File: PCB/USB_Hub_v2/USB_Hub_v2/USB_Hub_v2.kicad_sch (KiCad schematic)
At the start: 45 parts, among them J1 USB_A, J2 USB_A, J3 USB_A, J4 USB_A, J5 USB_A, J6 USB_A, SW1 SW_Push_DPDT, U1 FE1.1s, U2 TS3USB30EDGSR, U3 TPS2116DRL, U4 USBLC6-2SC6, U5 USBLC6-2SC6, U6 USBLC6-2SC6, U7 USBLC6-2SC6, U8 USBLC6-2SC6, U9 USBLC6-2SC6, Y1 Crystal

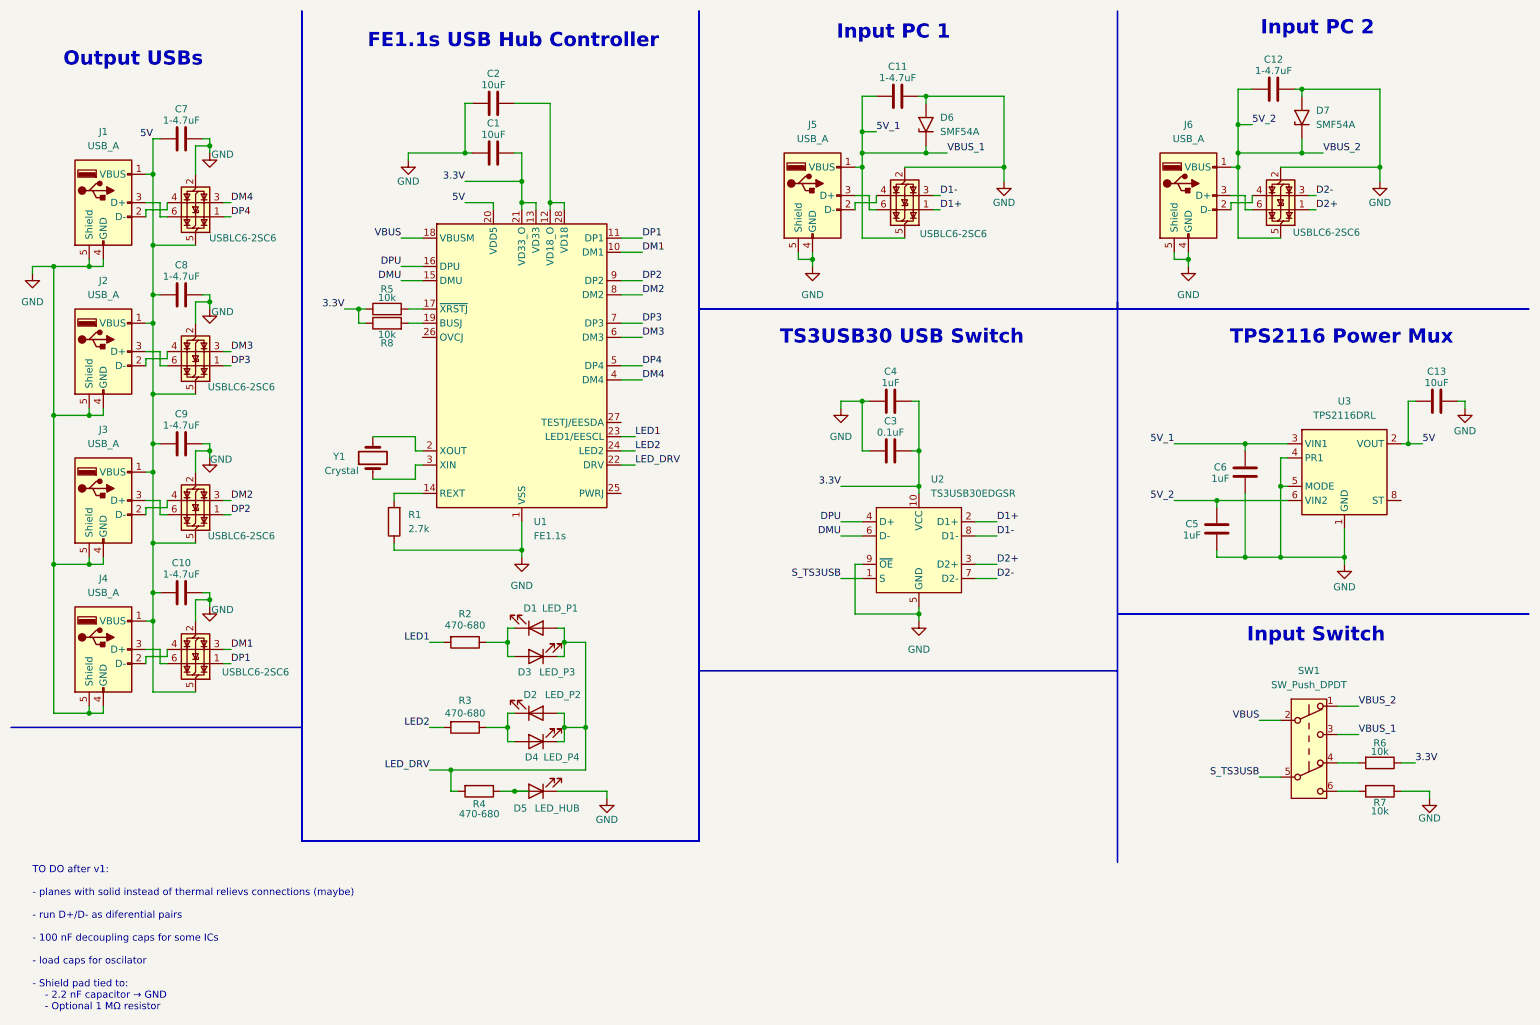
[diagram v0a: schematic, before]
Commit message: Update PCB layout: stackup, nets and footprints
Add recent PCB backup archives and apply extensive KiCad PCB updates: define board stackup and layer types (B.Cu -> power), rename/reorder nets, and replace/update multiple footprints and component properties (resistors, capacitors, pads, models, references and values). Adjust pad positions, sizes and net assignments, update 3D model links and footprint metadata to match revised layout. These changes appear to be automated footprint/housekeeping edits and netlist/stack adjustments to prepare the board for updated fabrication/assembly.
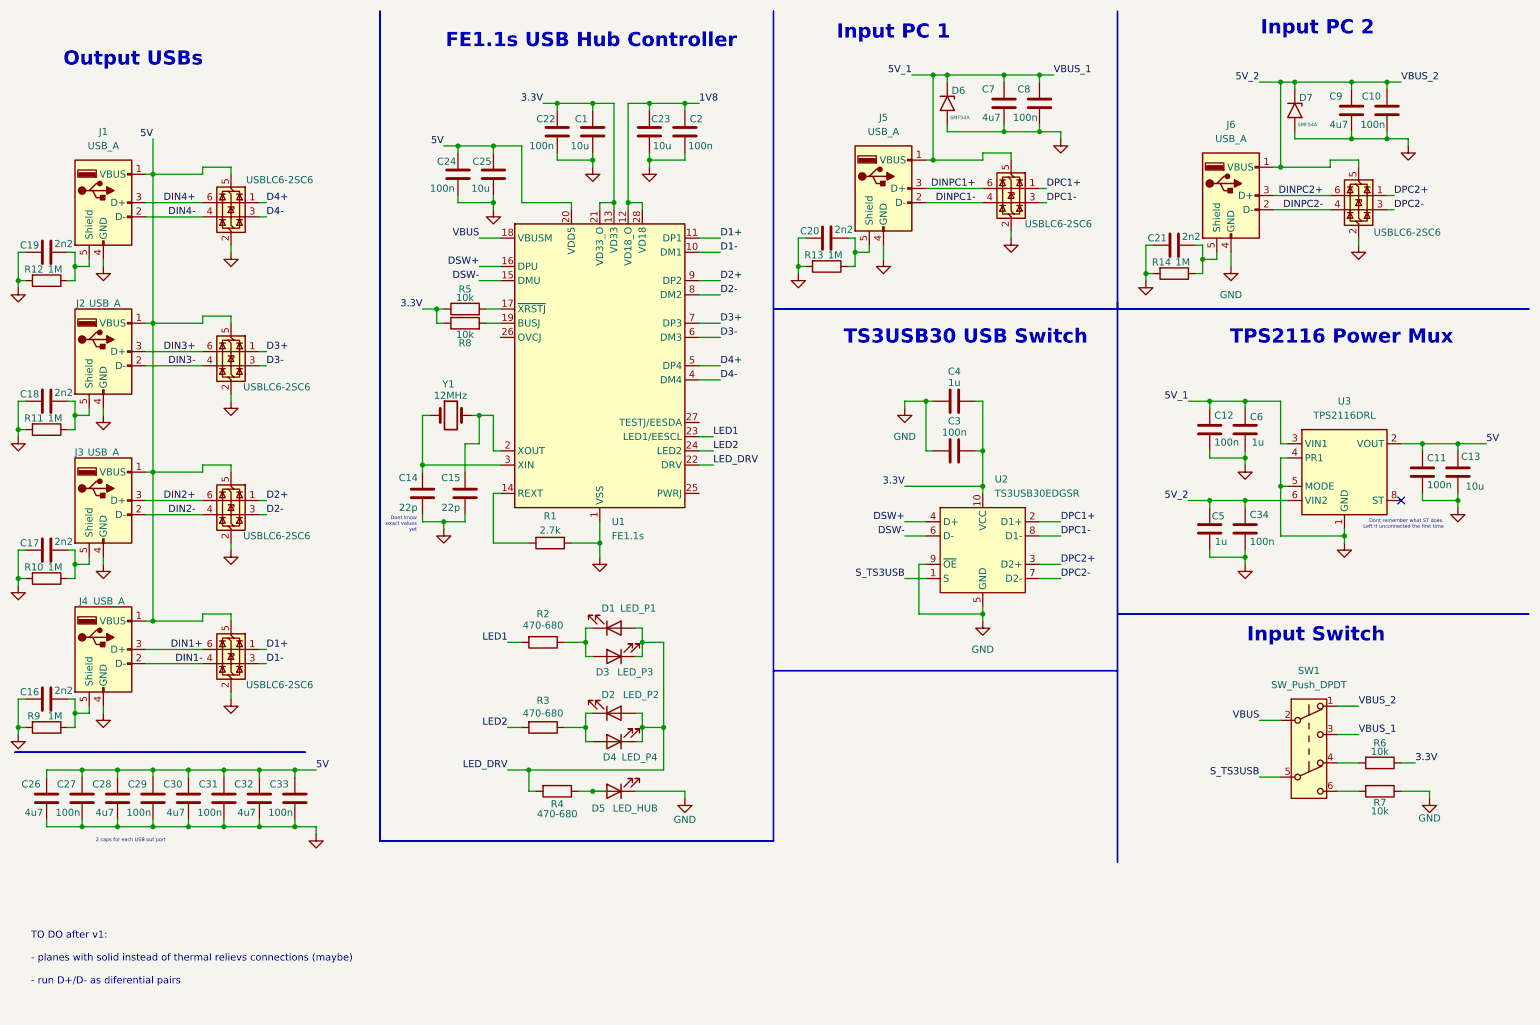
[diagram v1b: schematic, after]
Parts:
- added C14, C15: 22p, Capacitor_SMD:C_0805_2012Metric_Pad1.18x1.45mm_HandSolder, symbol Device:C
- added C16, C17, C18, C19, C20, C21: 2n2, Capacitor_SMD:C_0805_2012Metric_Pad1.18x1.45mm_HandSolder, symbol Device:C
- added C22, C24, C27, C29, C31, C33, C34: 100n, Capacitor_SMD:C_0805_2012Metric_Pad1.18x1.45mm_HandSolder, symbol Device:C
- added C23, C25: 10u, Capacitor_SMD:C_0805_2012Metric_Pad1.18x1.45mm_HandSolder, symbol Device:C
- added C26, C28, C30, C32: 4u7, Capacitor_SMD:C_0805_2012Metric_Pad1.18x1.45mm_HandSolder, symbol Device:C
- added R10, R11, R12, R13, R14, R9: 1M, Resistor_SMD:R_0603_1608Metric_Pad0.98x0.95mm_HandSolder, symbol Device:R
- C1, C13: value 10uF -> 10u
- C10, C11, C12, C8: value 1-4.7uF -> 100n
- C2: value 10uF -> 100n
- C3: value 0.1uF -> 100n
- C4, C5, C6: value 1uF -> 1u
- C7, C9: value 1-4.7uF -> 4u7
- Y1: value Crystal -> 12MHz
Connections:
- net DM1 is gone; now on net D1-: U1.10 (DM1), U7.3 (I/O2)
- net DM2 is gone; now on net D2-: U1.8 (DM2), U6.3 (I/O2)
- net DP1 is gone; now on net D1+: U1.11 (DP1), U7.1 (I/O1)
- net DP2 is gone; now on net D2+: U1.9 (DP2), U6.1 (I/O1)
- net 3.3V: now also C22.2
- net 5V: now also C11.1, C13.2, C24.2, C25.2, C26.2, C27.2, C28.2, C29.2, C30.2, C31.2, C32.2, C33.2; no longer C10.1, C13.1, C7.1, C8.1, C9.1
- net 5V_1: now also C12.1, C7.2, C8.2; no longer C11.1
- net 5V_2: now also C10.2, C9.2, C34.1; no longer C12.1
- net D1+: no longer U2.2 (D1+), U8.1 (I/O1)
- net D1-: no longer U2.8 (D1-), U8.3 (I/O2)
- net D2+: no longer U2.3 (D2+), U9.1 (I/O1)
- net D2-: no longer U2.7 (D2-), U9.3 (I/O2)
- net GND: now also C10.1, C13.1, C7.1, C8.1, C9.1, C14.1, C15.1, C16.1, C17.1, C18.1, C19.1, C20.1, C21.1, C22.1, C23.1, C24.1, C25.1, C26.1, C27.1, C28.1, C29.1, C30.1, C31.1, C32.1, C33.1, C34.2, R10.2, R11.2, R12.2, R13.2, R14.2, R9.2; no longer C10.2, C13.2, C7.2, C8.2, C9.2, J1.5 (Shield), J2.5 (Shield), J3.5 (Shield), J4.5 (Shield), J5.5 (Shield), J6.5 (Shield)
- net DINPC2-: now reaches J6.2 (D-), U9.4 (I/O2)
- net DINPC2+: now reaches J6.3 (D+), U9.6 (I/O1)
- net 1V8: now reaches C2.2, U1.12 (VD18_O), U1.28 (VD18)
- net 1V8: now also C23.2
- net DIN2-: now reaches J3.2 (D-), U6.4 (I/O2)
- net DIN2+: now reaches J3.3 (D+), U6.6 (I/O1)
- net DIN3-: now reaches J2.2 (D-), U5.4 (I/O2)
- net DIN3+: now reaches J2.3 (D+), U5.6 (I/O1)
- net DINPC1-: now reaches J5.2 (D-), U8.4 (I/O2)
- net DINPC1+: now reaches J5.3 (D+), U8.6 (I/O1)
- net at U1.2 (XOUT), Y1.2: now also C15.2
- net at U1.3 (XIN), Y1.1: now also C14.2
- net DIN1-: now reaches J4.2 (D-), U7.4 (I/O2)
- net DIN1+: now reaches J4.3 (D+), U7.6 (I/O1)
- net DIN4-: now reaches J1.2 (D-), U4.4 (I/O2)
- net DIN4+: now reaches J1.3 (D+), U4.6 (I/O1)
- net DM3 renamed D3-
- net DM4 renamed D4-
- net DMU renamed DSW-
- net DP3 renamed D3+
- net DP4 renamed D4+
- net DPU renamed DSW+
- new net: C17.2, J3.5 (Shield), R10.1
- new net: C21.2, J6.5 (Shield), R14.1
- new net: C20.2, J5.5 (Shield), R13.1
- new net: C16.2, J4.5 (Shield), R9.1
- new net: C18.2, J2.5 (Shield), R11.1
- new net: C19.2, J1.5 (Shield), R12.1
- new net DPC1+: U2.2 (D1+), U8.1 (I/O1)
- new net DPC1-: U2.8 (D1-), U8.3 (I/O2)
- new net DPC2+: U2.3 (D2+), U9.1 (I/O1)
- new net DPC2-: U2.7 (D2-), U9.3 (I/O2)
- no-connect marks 0 -> 1
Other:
- note added: "2 caps for each USB out port"
- note added: "Dont know exact values yet"
- note added: "Dont remember what ST does. Left it unconnected the first time"
- note added: "TO DO after v1: - planes with solid instead of thermal relievs connections (maybe) - run D+/D- as diferential pairs"
- note removed: "TO DO after v1: - planes with solid instead of thermal relievs connections (maybe) - run D+/D- as diferential pairs - 100 nF decoupling caps for some ICs - load caps for oscilator - Shield pad tied to: - 2.2 nF capacitor → GND - Optional 1 MΩ resistor"
- moved on the sheet: C1, C13, C3, C4, C5, C6, D1, D2, D3, D4, D5, D6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

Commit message: Adjust KiCad footprints and add backups
Rotate/reposition multiple SMD footprints, update pad rotations, fp_line/fp_text orientations and UUIDs in USB_Hub_v2.kicad_pcb (and related project files). Also update USB_Hub_v2.kicad_pro/.kicad_sch metadata to match footprint changes. Add five timestamped backup ZIPs under USB_Hub_v2-backups. These edits correct component orientations/placements and record backups.
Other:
- moved on the sheet: C2, C23
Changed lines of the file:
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@@
 	(symbol
 		(lib_id "Device:C")
-		(at 127 34.29 0)
+		(at 133.35 34.29 0)
 		(mirror x)
 		(unit 1)
@@
 		(dnp no)
 		(property "Reference" "C23"
-			(at 129.032 32.004 0)
+			(at 135.382 32.004 0)
 			(effects
 				(font
@@
 		)
 		(property "Value" "10u"
-			(at 129.286 36.83 0)
+			(at 135.636 36.83 0)
 			(effects
 				(font
@@
 		)
 		(property "Footprint" "Capacitor_SMD:C_0805_2012Metric_Pad1.18x1.45mm_HandSolder"
-			(at 127.9652 30.48 0)
+			(at 134.3152 30.48 0)
 			(effects
 				(font
@@
 		)
 		(property "Datasheet" "~"
-			(at 127 34.29 0)
+			(at 133.35 34.29 0)
 			(effects
 				(font
@@
 		)
 		(property "Description" "Unpolarized capacitor"
-			(at 127 34.29 0)
+			(at 133.35 34.29 0)
 			(effects
 				(font
@@
 	(symbol
 		(lib_id "Device:C")
-		(at 133.35 34.29 0)
+		(at 127 34.29 0)
 		(mirror x)
 		(unit 1)
@@
 		(dnp no)
 		(property "Reference" "C2"
-			(at 135.382 32.004 0)
+			(at 129.032 32.004 0)
 			(effects
 				(font
@@
 		)
 		(property "Value" "100n"
-			(at 136.144 36.83 0)
+			(at 129.794 36.83 0)
 			(effects
 				(font
@@
 		)
 		(property "Footprint" "Capacitor_SMD:C_0805_2012Metric_Pad1.18x1.45mm_HandSolder"
-			(at 134.3152 30.48 0)
+			(at 127.9652 30.48 0)
 			(effects
 				(font
@@
 		)
 		(property "Datasheet" "~"
-			(at 133.35 34.29 0)
+			(at 127 34.29 0)
 			(effects
 				(font
@@
 		)
 		(property "Description" "Unpolarized capacitor"
-			(at 133.35 34.29 0)
-			(effects
-				(font
+			(at 127 34.29 0)
+			(effects
+				(font

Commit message: Update KiCad PCB footprints, nets & backups
Enable dielectric constraints and introduce Net-(U2-S) (net 58); correct several pad/net assignments to use Net-(U2-S) instead of the old net, and update many footprint positions, rotations, silk/fab text orientations and UUIDs. Add a new C35 0805 capacitor footprint and other resized/rotated SMD footprints (resistors, caps), plus layout refinements. Also remove older backup ZIPs and add new backup archives. These changes adjust component placement/orientation and net mapping to match the updated board layout.
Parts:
- added C35: 100n, Capacitor_SMD:C_0805_2012Metric_Pad1.18x1.45mm_HandSolder, symbol Device:C
- added R15: 1k, Resistor_SMD:R_0603_1608Metric_Pad0.98x0.95mm_HandSolder, symbol Device:R
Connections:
- net GND: now also C35.1
- net S_TS3USB: now also R15.2; no longer U2.1 (S)
- new net: C35.2, R15.1, U2.1 (S)
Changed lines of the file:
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@@
 	)
 	(junction
+		(at 171.45 114.3)
+		(diameter 0)
+		(color 0 0 0 0)
+	)
+	(junction
 		(at 38.1 148.59)
 		(diameter 0)
@@
 	(wire
 		(pts
+			(xy 170.18 114.3) (xy 171.45 114.3)
+		)
+		(stroke
+			(width 0)
+			(type default)
+		)
+	)
+	(wire
+		(pts
 			(xy 176.53 111.76) (xy 175.26 111.76)
 		)
@@
 	(wire
 		(pts
+			(xy 171.45 114.3) (xy 176.53 114.3)
+		)
+		(stroke
+			(width 0)
+			(type default)
+		)
+	)
+	(wire
+		(pts
 			(xy 266.7 152.4) (xy 261.62 152.4)
 		)
@@
 	(wire
 		(pts
+			(xy 171.45 123.19) (xy 171.45 124.46)
+		)
+		(stroke
+			(width 0)
+			(type default)
+		)
+	)
+	(wire
+		(pts
 			(xy 15.24 109.22) (xy 13.97 109.22)
 		)
@@
 	(wire
 		(pts
+			(xy 171.45 114.3) (xy 171.45 115.57)
+		)
+		(stroke
+			(width 0)
+			(type default)
+		)
+	)
+	(wire
+		(pts
 			(xy 50.8 158.75) (xy 57.15 158.75)
 		)
@@
 	(wire
 		(pts
-			(xy 172.72 114.3) (xy 176.53 114.3)
-		)
-		(stroke
-			(width 0)
-			(type default)
-		)
-	)
-	(wire
-		(pts
 			(xy 231.14 55.88) (xy 231.14 58.42)
 		)
@@
 	(wire
 		(pts
+			(xy 161.29 114.3) (xy 162.56 114.3)
+		)
+		(stroke
+			(width 0)
+			(type default)
+		)
+	)
+	(wire
+		(pts
 			(xy 228.6 57.15) (xy 226.06 57.15)
 		)
@@
 	)
 	(label "S_TS3USB"
-		(at 172.72 114.3 180)
+		(at 161.29 114.3 180)
 		(effects
 			(font
@@
 					(size 1.27 1.27)
 				)
+				(hide yes)
 			)
 		)
@@
 	(symbol
 		(lib_id "power:GND")
+		(at 171.45 124.46 0)
+		(unit 1)
+		(exclude_from_sim no)
+		(in_bom yes)
+		(on_board yes)
+		(dnp no)
+		(fields_autoplaced yes)
+		(property "Reference" "#PWR035"
+			(at 171.45 130.81 0)
+			(effects
+				(font
+					(size 1.27 1.27)
+				)
+				(hide yes)
+			)
+		)
+		(property "Value" "GND"
+			(at 171.45 129.54 0)
+			(effects
+				(font
+					(size 1.27 1.27)
+				)
+				(hide yes)
+			)
+		)
+		(property "Footprint" ""
+			(at 171.45 124.46 0)
+			(effects
+				(font
+					(size 1.27 1.27)
+				)
+				(hide yes)
+			)
+		)
+		(property "Datasheet" ""
+			(at 171.45 124.46 0)
+			(effects
+				(font
+					(size 1.27 1.27)
+				)
+				(hide yes)
+			)
+		)
+		(property "Description" "Power symbol creates a global label with name \"GND\" , ground"
+			(at 171.45 124.46 0)
+			(effects
+				(font
+					(size 1.27 1.27)
+				)
+				(hide yes)
+			)
+		)
+		(pin "1"
+		)
+		(instances
+			(project "USB_Hub_v2"
+				(path "/9578ac23-9c49-4eaa-9f79-4eba038e5099"
+					(reference "#PWR035")
+					(unit 1)
+				)
+			)
+		)
+	)
+	(symbol
+		(lib_id "power:GND")
 		(at 67.31 160.02 0)
 		(unit 1)
@@
 	)
 	(symbol
+		(lib_id "Device:C")
+		(at 171.45 119.38 180)
+		(unit 1)
+		(exclude_from_sim no)
+		(in_bom yes)
+		(on_board yes)
+		(dnp no)
+		(property "Reference" "C35"
+			(at 168.91 117.094 0)
+			(effects
+				(font
+					(size 1.27 1.27)
+				)
+			)
+		)
+		(property "Value" "100n"
+			(at 168.402 121.666 0)
+			(effects
+				(font
+					(size 1.27 1.27)
+				)
+			)
+		)
+		(property "Footprint" "Capacitor_SMD:C_0805_2012Metric_Pad1.18x1.45mm_HandSolder"
+			(at 170.4848 115.57 0)
+			(effects
+				(font
+					(size 1.27 1.27)
+				)
+				(hide yes)
+			)
+		)
+		(property "Datasheet" "~"
+			(at 171.45 119.38 0)
+			(effects
+				(font
+					(size 1.27 1.27)
+				)
+				(hide yes)
+			)
+		)
+		(property "Description" "Unpolarized capacitor"
+			(at 171.45 119.38 0)
+			(effects
+				(font
+					(size 1.27 1.27)
+				)
+				(hide yes)
+			)
+		)
+		(pin "1"
+		)
+		(pin "2"
+		)
+		(instances
+			(project "USB_Hub_v2"
+				(path "/9578ac23-9c49-4eaa-9f79-4eba038e5099"
+					(reference "C35")
+					(unit 1)
+				)
+			)
+		)
+	)
+	(symbol
 		(lib_id "power:GND")
 		(at 29.21 111.76 0)
@@
 					(unit 1)
 				)
+			)
+		)
+	)
+	(symbol
+		(lib_id "Device:R")
+		(at 166.37 114.3 270)
+		(unit 1)
+		(exclude_from_sim no)
+		(in_bom yes)
+		(on_board yes)
+		(dnp no)
+		(property "Reference" "R15"
+			(at 164.338 112.268 90)
+			(effects
+				(font
+					(size 1.27 1.27)
+				)
+			)
+		)
+		(property "Value" "1k"
+			(at 169.418 112.268 90)
+			(effects
+				(font
+					(size 1.27 1.27)
+				)
+			)
+		)
+		(property "Footprint" "Resistor_SMD:R_0603_1608Metric_Pad0.98x0.95mm_HandSolder"
+			(at 166.37 112.522 90)
+			(effects
+				(font
+					(size 1.27 1.27)
+				)
+				(hide yes)
+			)
+		)
+		(property "Datasheet" "~"
+			(at 166.37 114.3 0)
+			(effects
+				(font
+					(size 1.27 1.27)
+				)
+				(hide yes)
+			)
+		)
+		(property "Description" "Resistor"
+			(at 166.37 114.3 0)
+			(effects
+				(font
+					(size 1.27 1.27)
+				)
+				(hide yes)
+			)
+		)
+		(pin "2"
+		)
+		(pin "1"
+		)
+		(instances
+			(project "USB_Hub_v2"
+				(path "/9578ac23-9c49-4eaa-9f79-4eba038e5099"
+					(reference "R15")
+					(unit 1)
+				)

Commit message: Update PCB layout: reroute nets and add backups
Add multiple USB_Hub_v2 backup zip snapshots and update KiCad project files. USB_Hub_v2.kicad_pcb: swap DPC1/DPC2 net assignments, hide C9 silkscreen reference, and apply extensive track/via repositioning and rerouting (many segment coordinate/width and via size/position adjustments and UUID updates). Also modify the project and schematic files (.kicad_pro, .kicad_sch) to reflect these PCB changes.
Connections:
- net DPC1+: now also U2.3 (D2+); no longer U2.2 (D1+)
- net DPC1-: now also U2.7 (D2-); no longer U2.8 (D1-)
- net DPC2+: now also U2.2 (D1+); no longer U2.3 (D2+)
- net DPC2-: now also U2.8 (D1-); no longer U2.7 (D2-)
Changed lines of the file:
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@@
 	)
 	(label "DPC2-"
-		(at 200.66 114.3 0)
+		(at 200.66 106.68 0)
 		(effects
 			(font
@@
 	)
 	(label "DPC1+"
-		(at 200.66 104.14 0)
+		(at 200.66 111.76 0)
 		(effects
 			(font
@@
 	)
 	(label "DPC2+"
-		(at 200.66 111.76 0)
+		(at 200.66 104.14 0)
 		(effects
 			(font
@@
 	)
 	(label "DPC1-"
-		(at 200.66 106.68 0)
-		(effects
-			(font
+		(at 200.66 114.3 0)
+		(effects
+			(font
